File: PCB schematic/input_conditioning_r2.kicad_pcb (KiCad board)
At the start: 4 copper layers, 194.5 x 113 mm, 60 parts, among them J3 Conn_Coaxial_x2, J4 Conn_01x02_Socket, J6 Conn_01x01_Socket, J7 Conn_01x08_Socket, J8 Conn_01x01_Socket, J9 Conn_01x01_Socket, SW1 Shifting, SW2 Scaling, SW3 Trigger, U1 OPA2365AID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

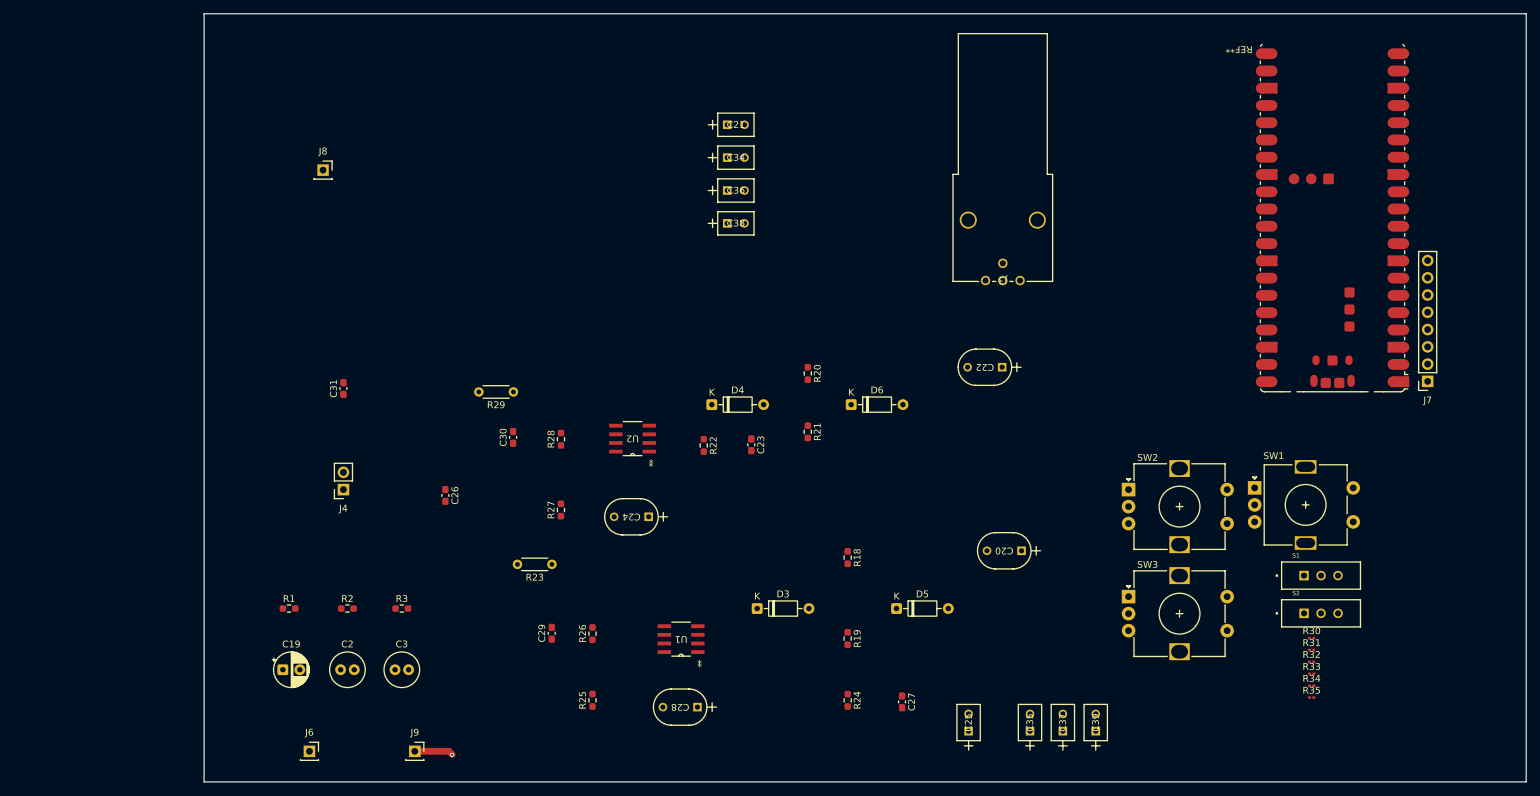
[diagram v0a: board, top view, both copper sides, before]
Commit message: schematic layout mostly done
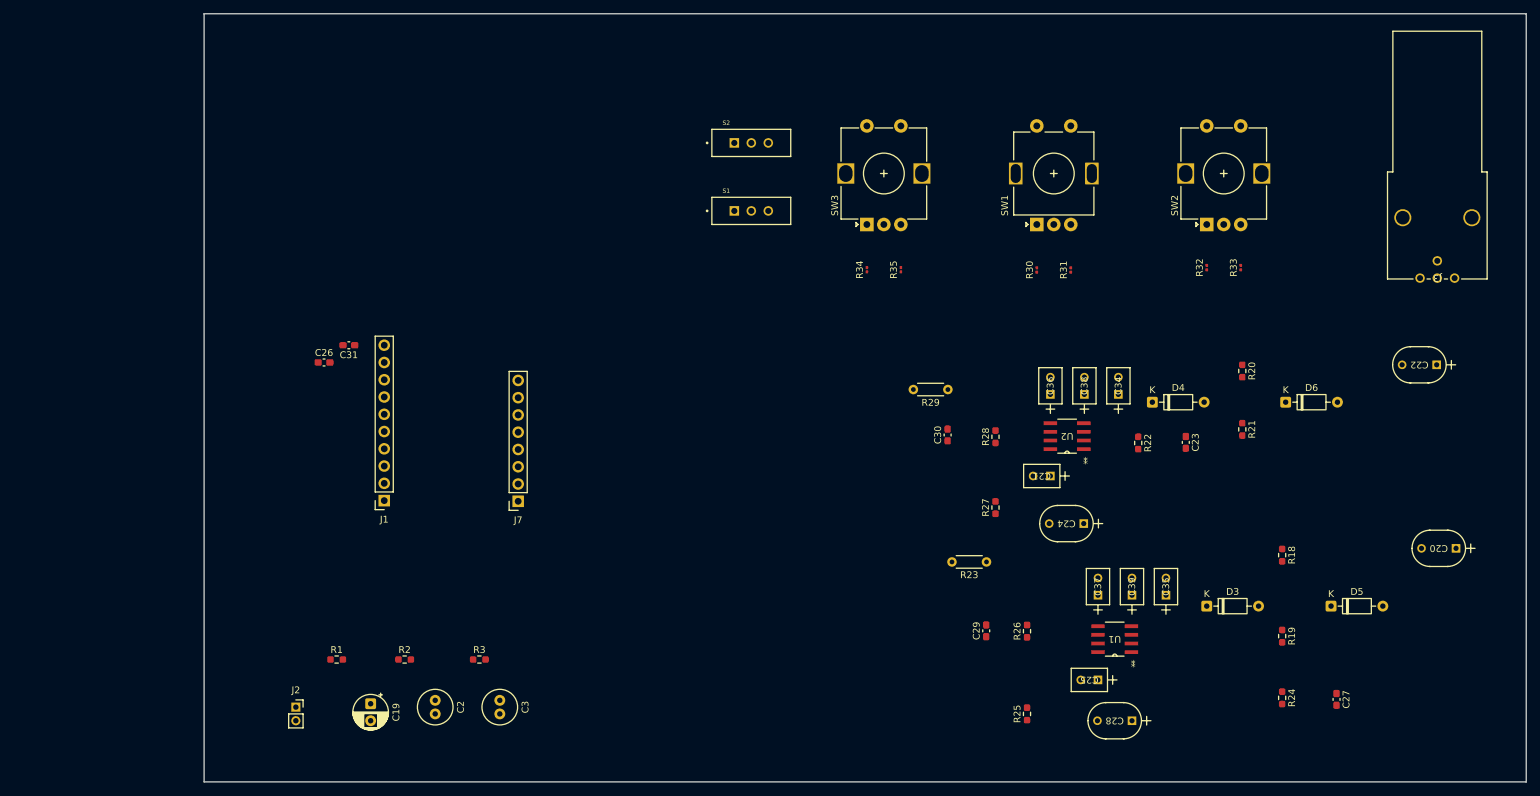
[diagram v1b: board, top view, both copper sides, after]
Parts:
- removed J4: Conn_01x02_Socket, Connector_PinSocket_2.54mm:PinSocket_1x02_P2.54mm_Vertical
- removed J6, J8, J9: Conn_01x01_Socket, Connector_PinSocket_2.54mm:PinSocket_1x01_P2.54mm_Vertical
- removed REF**: RaspberryPi_Pico_W_SMD, Module:RaspberryPi_Pico_W_SMD
- added J1: Conn_01x10_Socket, Connector_PinSocket_2.54mm:PinSocket_1x10_P2.54mm_Vertical, F.Cu at (94.0, 119.6)
- added J2: Conn_01x02_Socket, Connector_PinSocket_2.00mm:PinSocket_1x02_P2.00mm_Vertical, F.Cu at (81.0, 150.0)
- moved J7 135.0 mm to (113.7, 119.7)
- moved S2 108.7 mm to (148.0, 67.0)
- moved S1 99.5 mm to (148.0, 77.0)
- moved R34 89.6 mm to (165.0, 85.7), turned to 90 degrees
- moved R35 87.3 mm to (170.0, 85.7), turned to 90 degrees
- moved C21 70.2 mm to (192.0, 116.0), turned to 180 degrees
- moved R30 67.6 mm to (190.0, 85.7), turned to 90 degrees
- moved C34 67.3 mm to (202.0, 104.0), turned to 90 degrees
- moved SW3 66.9 mm to (165.0, 79.0), turned to 90 degrees
- moved R31 66.2 mm to (195.0, 85.7), turned to 90 degrees
- moved D3 66.1 mm to (215.0, 135.1)
- moved D4 64.8 mm to (207.0, 105.1)
- moved C24 64.0 mm to (196.9, 123.0)
- moved C28 64.0 mm to (204.0, 152.0)
- moved R25 64.0 mm to (188.6, 151.0)
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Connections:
- net /User Interface/V3.3 renamed +3V3
- C34 pad 1: +5V -> +2V5
- C35 pad 1: +5V -> +2V5
- C36 pad 1: +5V -> /+1V25
- C37 pad 1: +5V -> /+1V25
- C38 pad 1: +5V -> GND
- C39 pad 1: +5V -> GND
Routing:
- net GND: track 5.71 -> 0.00 mm, vias 1 -> 0
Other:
- board text removed: "3.3V In"
- board text removed: "5V in"
- board text removed: "GND"
- board text removed: "Signal Outs"

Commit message: "Updated UI part of PCB"
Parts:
- moved SW2 79.4 mm to (136.0, 86.5)
- moved R33 64.2 mm to (156.5, 95.1)
- moved R32 61.8 mm to (154.0, 95.1)
- moved C26 51.2 mm to (124.3, 132.4), turned to 90 degrees
- moved J1 50.8 mm to (144.6, 123.5), turned to -90 degrees
- moved SW3 48.0 mm to (117.5, 86.0)
- moved C31 45.9 mm to (121.8, 128.7), turned to -90 degrees
- moved S1 45.5 mm to (103.0, 84.0)
- moved S2 45.4 mm to (103.0, 73.0)
- moved SW1 36.3 mm to (154.5, 86.5)
- moved J7 34.9 mm to (144.7, 103.8), turned to -90 degrees
- moved R31 33.3 mm to (163.0, 95.0)
- moved R30 30.9 mm to (160.5, 95.0)
- moved R35 23.0 mm to (149.0, 95.2)
- moved R34 21.2 mm to (146.0, 95.2)

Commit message: pcb initial complete revision
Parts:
- moved J3 194.7 mm to (56.0, 113.3), turned to 0 degrees
- moved C20 181.9 mm to (70.1, 138.0), turned to 0 degrees
- moved C22 177.3 mm to (78.0, 147.0), turned to 0 degrees
- moved D5 162.7 mm to (71.0, 123.0), turned to -90 degrees
- moved R18 150.1 mm to (76.0, 131.0), turned to 90 degrees
- moved C27 149.2 mm to (89.0, 114.0), turned to 90 degrees
- moved R19 142.6 mm to (85.1, 118.0), turned to 0 degrees
- moved D6 141.5 mm to (89.0, 138.0), turned to 90 degrees
- moved R20 141.4 mm to (85.1, 142.0), turned to 0 degrees
- moved R24 136.6 mm to (94.0, 113.9), turned to 90 degrees
- moved D3 133.1 mm to (82.0, 130.6), turned to 90 degrees
- moved R21 130.5 mm to (93.9, 142.0), turned to 0 degrees
- moved D4 117.7 mm to (96.6, 146.0), turned to 180 degrees
- moved C35 116.3 mm to (93.0, 125.2), turned to -90 degrees
- moved C23 115.0 mm to (99.9, 137.0), turned to 0 degrees
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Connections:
- D3 pad 2: Net-(D3-A) -> /Real Signal Processing 1/ac_coupled
- D4 pad 2: Net-(D4-A) -> /Real Signal Processing 2/ac_coupled
- D5 pad 1: Net-(D3-A) -> /Real Signal Processing 1/ac_coupled
- D6 pad 1: Net-(D4-A) -> /Real Signal Processing 2/ac_coupled
- J1 pad 10: /output_2 -> /output_1
- J1 pad 9: /output_1 -> /output_2
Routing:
- net +3V3: track 0.00 -> 161.2 mm, vias 0 -> 3
- net Net-(J7-Pin_7): track 0.00 -> 147.3 mm
- net Net-(J7-Pin_6): track 0.00 -> 146.6 mm, vias 0 -> 2
- net Net-(J7-Pin_8): track 0.00 -> 146.1 mm
- net Net-(J7-Pin_5): track 0.00 -> 136.6 mm, vias 0 -> 2
- net Net-(J7-Pin_4): track 0.00 -> 131.3 mm, vias 0 -> 2
- net Net-(J7-Pin_3): track 0.00 -> 116.2 mm, vias 0 -> 2
- net Net-(J7-Pin_2): track 0.00 -> 115.1 mm, vias 0 -> 2
- net /+1V25: track 0.00 -> 110.2 mm
- net Net-(J7-Pin_1): track 0.00 -> 99.7 mm, vias 0 -> 2
- net +2V5: track 0.00 -> 96.5 mm
- net /input_2: track 0.00 -> 55.0 mm
- net /input_1: track 0.00 -> 45.5 mm
- net /Real Signal Processing 2/s2_in: track 0.00 -> 34.0 mm, vias 0 -> 2
- net /Real Signal Processing 1/s1_out: track 0.00 -> 33.1 mm
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- added copper zone on In2.Cu, net +5V
- added copper zone on In1.Cu, net GND
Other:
- board size 194.5 x 113 mm -> 125 x 96.4 mm
- board text added: "pico"
- board text removed: "BNC"

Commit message: pcb fixed encoder footprints
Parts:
- SW2, SW3: footprint Rotary_Encoder:RotaryEncoder_Alps_EC12E-Switch_Vertical_H20mm -> Rotary_Encoder:RotaryEncoder_Alps_EC11E-Switch_Vertical_H20mm

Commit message: pcb almost ready to order
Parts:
- J1: footprint Connector_PinSocket_2.54mm:PinSocket_1x10_P2.54mm_Vertical -> Connector_PinSocket_2.54mm:PinSocket_1x20_P2.54mm_Vertical
- J7: footprint Connector_PinSocket_2.54mm:PinSocket_1x08_P2.54mm_Vertical -> Connector_PinSocket_2.54mm:PinSocket_1x20_P2.54mm_Vertical
- R30, R31, R32, R33, R34, R35: footprint Resistor_SMD:R_0201_0603Metric -> Resistor_SMD:R_0805_2012Metric_Pad1.20x1.40mm_HandSolder
- moved R30 0.66 mm to (105.0, 110.0)
- moved R31 0.66 mm to (110.0, 110.0)
- moved R32 0.66 mm to (88.0, 110.0)
- moved R33 0.66 mm to (93.0, 110.0)
- moved R34 0.66 mm to (71.0, 110.0)
- moved R35 0.66 mm to (76.0, 110.0)
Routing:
- net +5V: track 17.7 -> 20.3 mm
- net Net-(J7-Pin_8): track 146.1 -> 144.7 mm
- net Net-(J7-Pin_6): track 146.6 -> 145.4 mm
- net Net-(J7-Pin_5): track 136.6 -> 135.3 mm
- net Net-(J7-Pin_3): track 116.2 -> 115.0 mm
- net Net-(J7-Pin_2): track 115.1 -> 113.8 mm
- net Net-(J7-Pin_1): track 99.7 -> 98.4 mm
- net Net-(J7-Pin_4): track 131.3 -> 130.0 mm
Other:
- board size 125 x 96.4 mm -> 118.5 x 67.5 mm

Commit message: pcb finished
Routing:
- net +3V3: track 161.3 -> 168.0 mm
- net Net-(J7-Pin_3): track 115.0 -> 119.5 mm
- net Net-(J7-Pin_2): track 113.8 -> 118.3 mm
- net Net-(J7-Pin_1): track 98.4 -> 103.0 mm
- net Net-(J7-Pin_4): track 130.0 -> 133.7 mm
- net Net-(J7-Pin_5): track 135.3 -> 139.0 mm
- net Net-(J7-Pin_6): track 145.4 -> 149.1 mm
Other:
- board text added: "Conn_01x10_Socket"
